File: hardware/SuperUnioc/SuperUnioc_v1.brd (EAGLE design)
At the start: 92.5 x 80 mm, 57 parts, among them IC1 MAX3232CSE, IC5 XMEGA128-A1

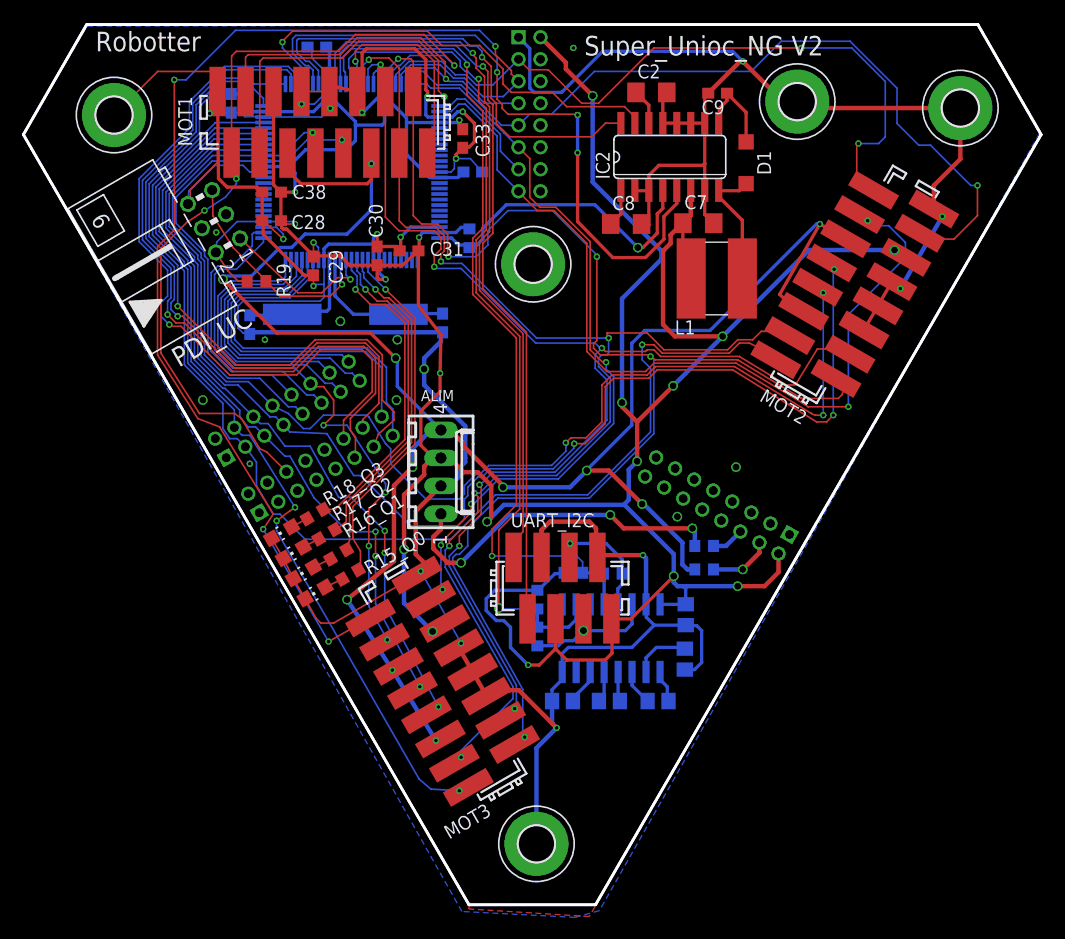
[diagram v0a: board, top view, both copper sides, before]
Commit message: super unioc: add GP2 connector
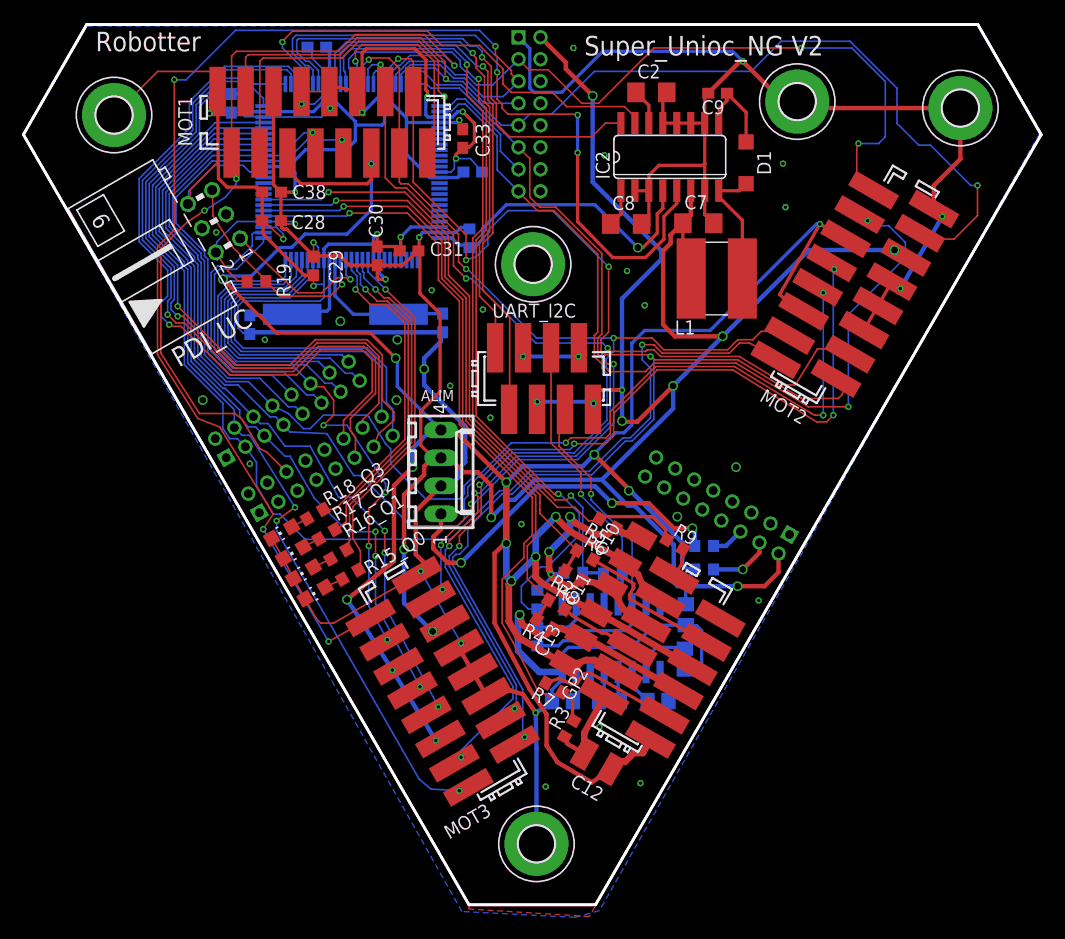
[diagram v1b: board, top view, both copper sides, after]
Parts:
- added C10, C11, C12, C13: 10UFC, robotter_capacitor:C1210
- added GP2: MICROMATCH-12_SMD, robotter_connector:MICROMATCH-12_SMD
- added R2, R3, R4, R5: 270-F, robotter_resistor:R0603
- added R6, R7, R8, R9: (no value), robotter_resistor:R0603
- moved UART_I2C 19.1 mm to (47.3, 47.8)
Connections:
- removed net ASD0: IC5.12
- removed net CONF_DONE: IC5.5
- removed net DATA0: IC5.9
- removed net DCLK: IC5.8
- removed net FPGA_IRQ_3V3: IC5.10
- removed net NCE: IC5.7
- removed net NCONFIG: IC5.6
- removed net NCS0: IC5.11
- new net GP2_0_0-1V: IC5.8, R5.2, R9.1
- new net GP2_1_0-1V: IC5.7, R2.2, R6.1
- new net GP2_2_0-1V: IC5.6, R4.2, R8.1
- new net GP2_3_0-1V: IC5.5, R3.2, R7.1
- new net N$22: GP2.1, R9.2
- new net N$24: GP2.7, R8.2
- new net N$36: GP2.10, R7.2
- new net N$37: GP2.4, R6.2
- net +3V3: no longer R21.2, R23.2
- net +5V: now also C10.1, C11.1, C12.1, C13.1, GP2.12, GP2.3, GP2.6, GP2.9
- net GND: now also C10.2, C11.2, C12.2, C13.2, GP2.11, GP2.2, GP2.5, GP2.8, R2.1, R21.2, R23.2, R3.1, R4.1, R5.1
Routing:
- net +5V: track 175.0 -> 270.5 mm, vias 11 -> 15
- net GP2_3_0-1V: track 0.00 -> 68.8 mm, vias 0 -> 1
- net GP2_0_0-1V: track 0.00 -> 59.7 mm, vias 0 -> 1
- net GP2_2_0-1V: track 0.00 -> 57.0 mm, vias 0 -> 1
- net GP2_1_0-1V: track 0.00 -> 53.6 mm, vias 0 -> 1
- net GND: track 415.3 -> 463.4 mm, vias 29 -> 47
- net +3V3: track 345.4 -> 323.2 mm, vias 19 -> 18
- net SDA_3V3: track 65.0 -> 44.6 mm
- net SCL_3V3: track 69.5 -> 49.8 mm
- net TX_232: track 12.3 -> 31.9 mm
- net RX_232: track 10.9 -> 26.2 mm
- net N$37: track 0.00 -> 13.8 mm
- net N$36: track 0.00 -> 12.4 mm
- net N$24: track 0.00 -> 7.14 mm
- net RX_3V3: track 77.2 -> 72.2 mm
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
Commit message: radiospares part number added
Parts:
- C10, C11, C12, C13: value 10UFC -> 10UF-C_25V

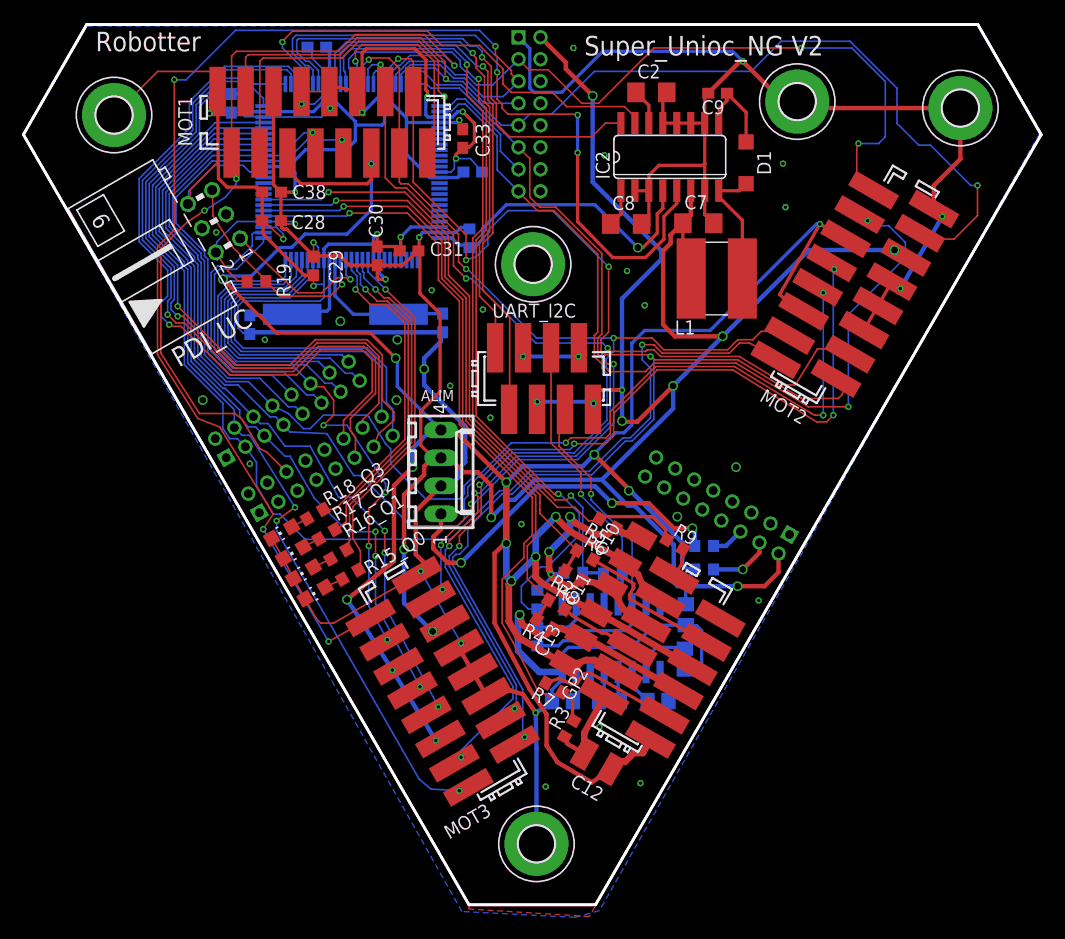
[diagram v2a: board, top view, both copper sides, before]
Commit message: ferrit bead on avcc added
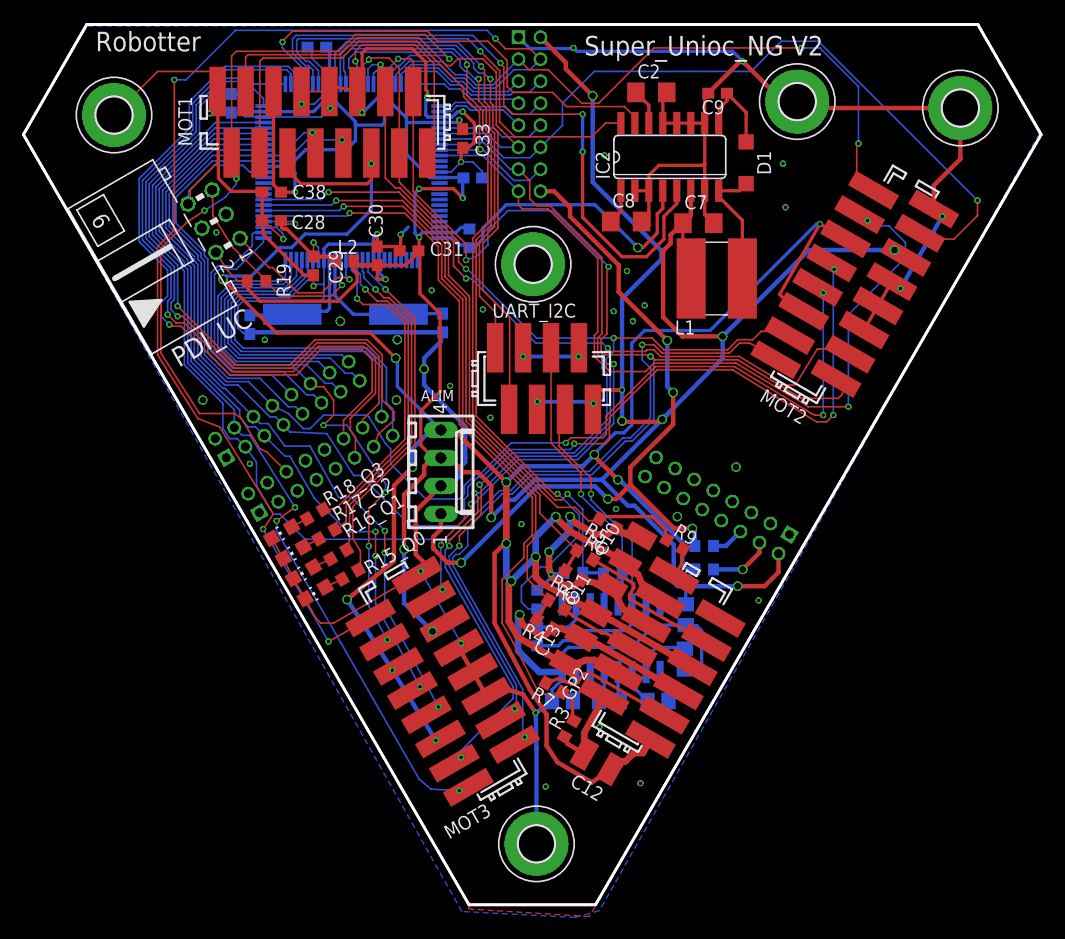
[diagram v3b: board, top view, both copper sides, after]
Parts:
- added L2: 220 ohms, robotter_inductor:R0603
- IC2: value (none) -> ADXRS453BRGZ
- moved C32 0.53 mm to (40.8, 66.1)
- moved C8 0.23 mm to (54.8, 62.1)
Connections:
- new net N$25: C28.1, C29.1, IC5.4, IC5.94, L2.1
- new net PF3: IC5.48, JA1.5
- new net PF4: IC5.49, JA1.6
- new net PF5: IC5.50, JA1.7
- new net PF6: IC5.51, JA1.8
- new net PF7: IC5.52, JA1.9
- new net PH0: IC5.55, JA1.10
- net +12V: now also JA1.16
- net +3V3: now also L2.2; no longer C28.1, C29.1, IC5.4, IC5.94
- net BRAKE_MOT0_3V3: now also IC5.59, JA1.14; no longer IC5.51, JA1.13
- net BRAKE_MOT1_3V3: now also IC5.60; no longer IC5.52
- net DIRECTION_MOT0_3V3: now also IC5.56, JA1.11; no longer IC5.48, JA1.7
- net DIRECTION_MOT1_3V3: now also IC5.57, JA1.12; no longer IC5.49, JA1.9
- net DIRECTION_MOT2_3V3: now also IC5.58, JA1.13; no longer IC5.50, JA1.11
- net PWM_MOT2_3V3: now also JA1.4; no longer JA1.5
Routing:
- net +12V: track 33.7 -> 68.7 mm, vias 3 -> 5
- net N$25: track 0.00 -> 14.1 mm, vias 0 -> 2
- net PF4: track 0.00 -> 14.1 mm
- net PF3: track 0.00 -> 12.6 mm
- net PF6: track 0.00 -> 10.2 mm
- net PH0: track 0.00 -> 9.95 mm
- net PF5: track 0.00 -> 9.91 mm
- net PF7: track 0.00 -> 8.13 mm
- net GND: track 463.4 -> 455.4 mm, vias 47 -> 50
- net DIRECTION_MOT0_3V3: track 37.1 -> 43.8 mm, vias 1 -> 0
- net DIRECTION_MOT2_3V3: track 68.1 -> 62.6 mm
- net DIRECTION_MOT1_3V3: track 73.9 -> 68.8 mm
- net BRAKE_MOT0_3V3: track 41.4 -> 46.3 mm
- net PWM_MOT1_3V3: track 65.5 -> 60.7 mm
- net BRAKE_MOT1_3V3: track 79.1 -> 75.5 mm
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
